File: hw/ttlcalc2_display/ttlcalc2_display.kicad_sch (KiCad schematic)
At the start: 21 parts, among them J1 DISP_CONN, J2 5V_PWR, J3 HV_PWR, J4 IO_BUS, Q1 MPSA42, Q2 MPSA42, Q3 MPSA42, U1 74LS93, U2 NE555P, U3 74LS08, U4 74LS139, U5 74LS173, U6 74LS138, U7 74LS173

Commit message: Continue work on display driver board schematic
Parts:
- added C50: 1000u, Capacitor_THT:CP_Radial_D10.0mm_P5.00mm, symbol Device:C_Polarized_US
- added C51: 100u, Capacitor_THT:CP_Radial_D18.0mm_P7.50mm, symbol Device:C_Polarized_US
- added U23: 74LS02, Package_DIP:DIP-14_W7.62mm, symbol 74xx:74LS02
- R1, R2, R3, R4, R5: footprint Resistor_THT:R_Axial_DIN0309_L9.0mm_D3.2mm_P2.54mm_Vertical -> Resistor_THT:R_Axial_DIN0207_L6.3mm_D2.5mm_P2.54mm_Vertical
- renumbered C1 to C101, C2 to C102, J4 to J2, J2 to J3, J3 to J4, U2 to U1, U1 to U2, U4 to U3, U6 to U4, U3 to U5, U5 to U6
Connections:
- net CLK2: now also U23.13; no longer J2.21 (Pin_21)
- net Digit Storage/~{WEN}: now also U23.4; no longer U3.4 (O0)
- net GND: now also C50.2, C51.2, U23.8
- net HT: now also C51.1
- net VCC: now also C50.1
- net CLK1: no longer names the net of J2.23 (Pin_23)
- net DI0: no longer names the net of J2.25 (Pin_25)
- net DI1: no longer names the net of J2.27 (Pin_27)
- net DI2: no longer names the net of J2.29 (Pin_29)
- net DI3: no longer names the net of J2.31 (Pin_31)
- net ~{RIO}: no longer names the net of J2.19 (Pin_19)
- new net: J2.21 (Pin_21), U23.9
- new net: U23.1, U23.5, U23.6
- new net: U23.3, U3.4 (O0)
- new net ~{CLK2}: U23.10, U23.11, U23.12, U23.2
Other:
- moved on the sheet: J2, J3, J4, U3A, U3B

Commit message: Simplify display driver board, add busy light
Removed digit storage and multiplexing logic from display driver, will handle in software instead
Add driver for busy indicator
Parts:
- removed C101: 10n, Capacitor_THT:C_Disc_D5.0mm_W2.5mm_P5.00mm, symbol Device:C
- removed C102: 47n, Capacitor_THT:C_Disc_D5.0mm_W2.5mm_P5.00mm, symbol Device:C
- removed C50: 1000u, Capacitor_THT:CP_Radial_D10.0mm_P5.00mm, symbol Device:C_Polarized_US
- removed C51: 100u, Capacitor_THT:CP_Radial_D18.0mm_P7.50mm, symbol Device:C_Polarized_US
- removed J3: 5V_PWR, TerminalBlock_Phoenix:TerminalBlock_Phoenix_MKDS-1,5-2-5.08_1x02_P5.08mm_Horizontal, symbol Connector_Generic:Conn_01x02
- removed J4: HV_PWR, TerminalBlock_Phoenix:TerminalBlock_Phoenix_MKDS-1,5-2-5.08_1x02_P5.08mm_Horizontal, symbol Connector_Generic:Conn_01x02
- removed R1: 39k, Resistor_THT:R_Axial_DIN0207_L6.3mm_D2.5mm_P2.54mm_Vertical, symbol Device:R_US
- removed R2: 3.3k, Resistor_THT:R_Axial_DIN0207_L6.3mm_D2.5mm_P2.54mm_Vertical, symbol Device:R_US
- removed U1: NE555P, Package_DIP:DIP-8_W7.62mm, symbol Timer:NE555P
- removed U2: 74LS93, Package_DIP:DIP-14_W7.62mm, symbol 74xx:74LS93
- removed U23: 74LS02, Package_DIP:DIP-14_W7.62mm, symbol 74xx:74LS02
- removed unit 4 of U5
- added Q4: MPSA42, Package_TO_SOT_THT:TO-92_Inline, symbol Transistor_BJT:MPSA42
- added R4: 27k, Resistor_THT:R_Axial_DIN0207_L6.3mm_D2.5mm_P2.54mm_Vertical, symbol Device:R_US
- added U3, U4: 74LS173, Package_DIP:DIP-16_W7.62mm, symbol 74xx:74LS173
- added unit 4 of U6
- renumbered R3 to R1, R4 to R2, R5 to R3, U3 to U1, U4 to U2, U7 to U5, U5 to U6, U6 to U7
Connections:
- net CLK2: now also U3.7 (Cp), U4.7 (Cp), U6.11
- net DO0: now also U3.14 (D0), U4.14 (D0)
- net DO1: now also U3.13 (D1), U4.13 (D1)
- net DO2: now also U3.12 (D2), U4.12 (D2)
- net DO3: now also U3.11 (D3), U4.11 (D3)
- net GND: now also Q4.1 (E), U3.1 (Oe1), U3.15 (Mr), U3.2 (Oe2), U3.8 (GND), U3.9 (E1), U4.1 (Oe1), U4.15 (Mr), U4.2 (Oe2), U4.8 (GND), U4.9 (E1)
- net NXSEL0: now also U3.3 (Q0)
- net NXSEL1: now also U3.4 (Q1)
- net NXSEL2: now also U3.5 (Q2)
- net NXSEL3: now also U3.6 (Q3)
- net VCC: now also U3.16 (VCC), U4.16 (VCC), U6.12
- net at U7.9 (E1): now also U2.13 (O2); no longer U2.15 (O0)
- net at J2.21 (Pin_21): now also U6.13
- net at U2.12 (O3): now also U5.9 (E1)
- net at U2.14 (O1): now also U4.10 (E2); no longer U5.9 (E1)
- net at U2.4 (E1): now also U1.4 (O0); no longer U1.5 (O1)
- net NE_BUSY: now reaches J1.40 (Pin_40)
- net NE_BUSY: now also Q4.3 (C)
- net BUSY: now reaches U5.6 (Q3)
- net BUSY: now also R4.1
- net Digit Storage/DOUT0 renamed Nixie Cathode Drive/NXD0
- net Nixie Cathode Drive/NXD0: now also U4.3 (Q0)
- net Digit Storage/DOUT1 renamed Nixie Cathode Drive/NXD1
- net Nixie Cathode Drive/NXD1: now also U4.4 (Q1)
- net Digit Storage/DOUT2 renamed Nixie Cathode Drive/NXD2
- net Nixie Cathode Drive/NXD2: now also U4.5 (Q2)
- net Digit Storage/DOUT3 renamed Nixie Cathode Drive/NXD3
- net Nixie Cathode Drive/NXD3: now also U4.6 (Q3)
- net Nixie Anode Drive/~{EN1} renamed Nixie Anode Drive/~{EN}
- new net: U2.15 (O0), U3.10 (E2)
- new net: Q4.2 (B), R4.2
- no-connect marks 20 -> 16
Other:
- removed sheet Digit Storage
- sheet Nixie Anode Drive ports: added ~{EN}; removed EN2, ~{EN1}
- moved on the sheet: Q1, Q2, Q3, R1, R2, R3, U1A, U1B, U2, U5

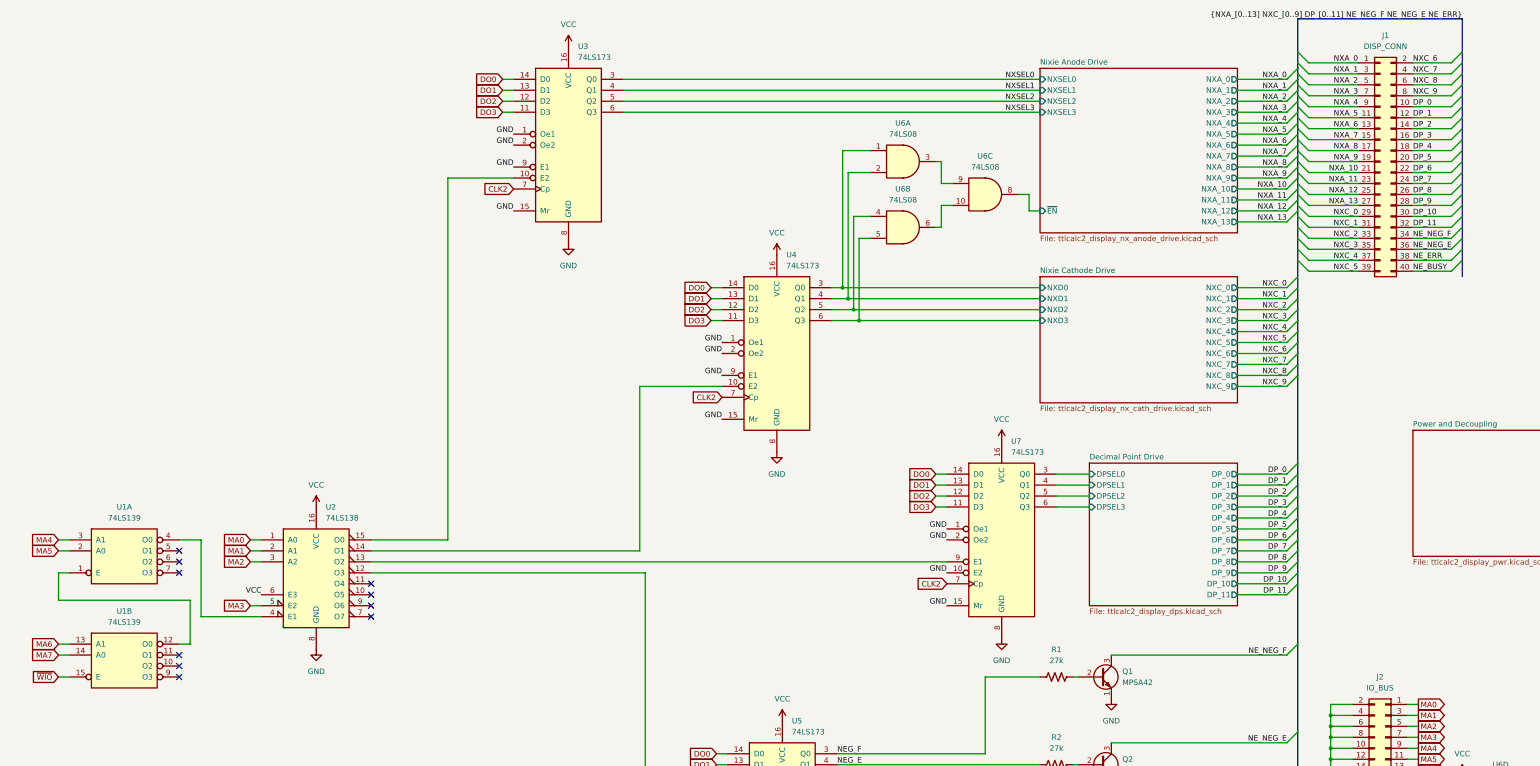
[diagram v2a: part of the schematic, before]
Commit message: Minor simplifications and ERC fix
Fix missing NE_BUSY from bus definition
Switch 74LS139 to 74LS138
Remove extra bypass caps
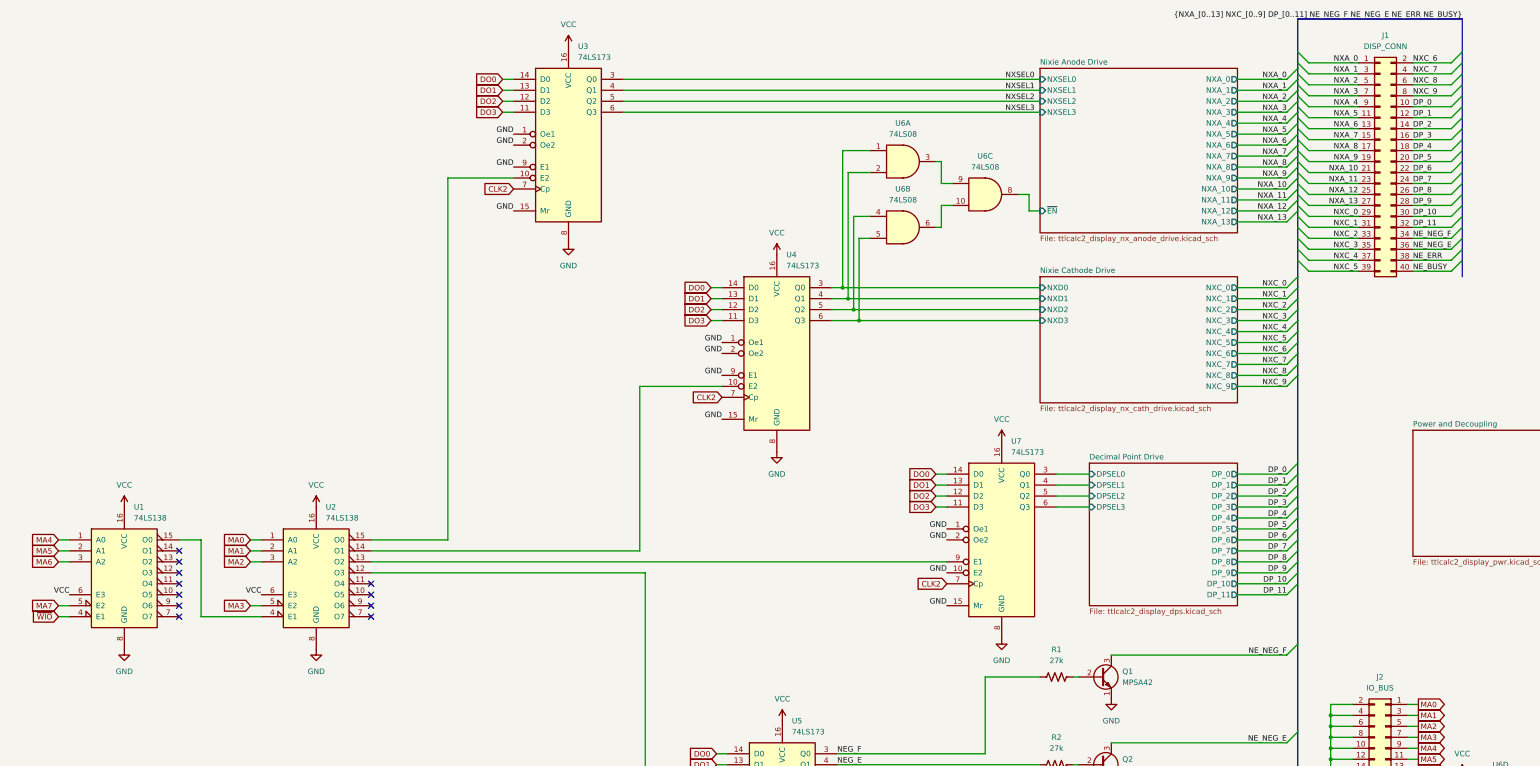
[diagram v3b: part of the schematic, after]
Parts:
- removed U1: 74LS139, Package_DIP:DIP-16_W7.62mm, symbol 74xx:74LS139
- added U1: 74LS138, Package_DIP:DIP-16_W7.62mm, symbol 74xx:74LS138
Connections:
- net GND: now also U1.8 (GND)
- net MA4: now also U1.1 (A0)
- net MA5: now also U1.2 (A1)
- net MA6: now also U1.3 (A2)
- net MA7: now also U1.5 (E2)
- net VCC: now also U1.16 (VCC), U1.6 (E3)
- net ~{WIO}: now also U1.4 (E1)
- net at U2.4 (E1): now also U1.15 (O0)
- no-connect marks 16 -> 17

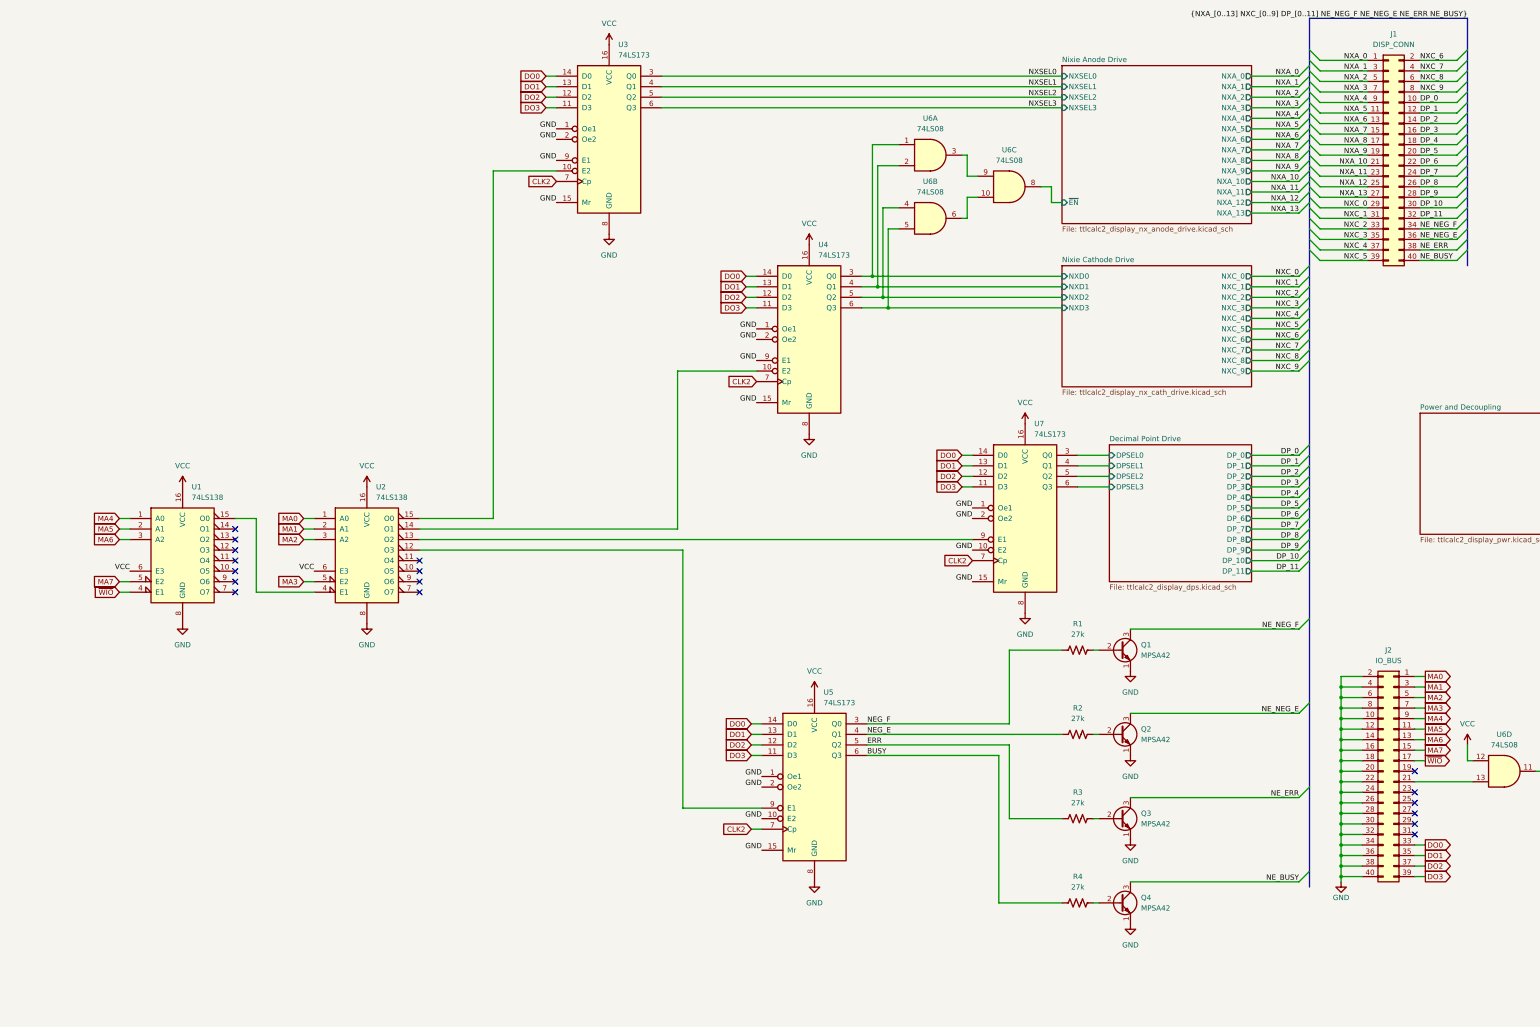
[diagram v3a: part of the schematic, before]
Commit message: Display driver board routing and silkscreen tweaks
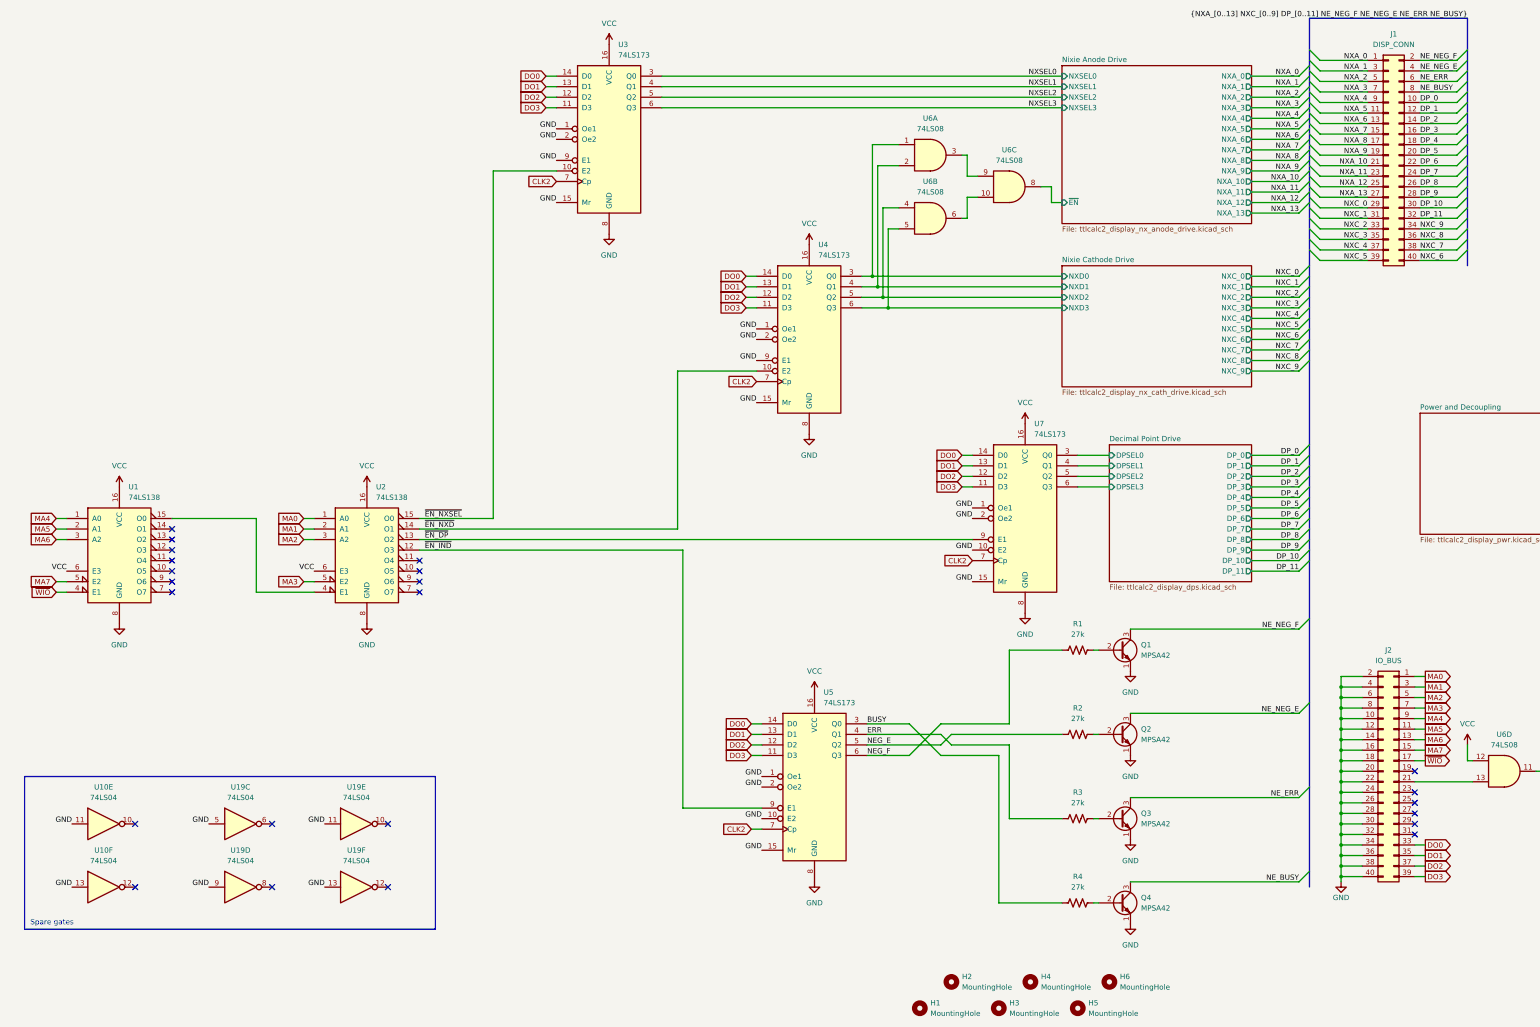
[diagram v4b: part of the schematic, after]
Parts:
- added H1, H2, H3, H4, H5, H6: MountingHole, MountingHole:MountingHole_3.2mm_M3, symbol Mechanical:MountingHole
- added U10, U19: 74LS04, Package_DIP:DIP-14_W7.62mm, symbol 74xx:74LS04
- J1: footprint Connector_PinHeader_2.54mm:PinHeader_2x20_P2.54mm_Vertical -> Connector_IDC:IDC-Header_2x20_P2.54mm_Vertical
- Q1, Q2, Q3, Q4: footprint Package_TO_SOT_THT:TO-92_Inline -> Package_TO_SOT_THT:TO-92_Inline_Wide
- R1, R2, R3, R4: footprint Resistor_THT:R_Axial_DIN0207_L6.3mm_D2.5mm_P2.54mm_Vertical -> Resistor_THT:R_Axial_DIN0207_L6.3mm_D2.5mm_P7.62mm_Horizontal
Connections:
- net BUSY: now also U5.3 (Q0); no longer U5.6 (Q3)
- net ERR: now also U5.4 (Q1); no longer U5.5 (Q2)
- net GND: now also U10.11, U10.13, U19.11, U19.13, U19.5, U19.9
- net NEG_E: now also U5.5 (Q2); no longer U5.4 (Q1)
- net NEG_F: now also U5.6 (Q3); no longer U5.3 (Q0)
- net NE_BUSY: now also J1.8 (Pin_8); no longer J1.40 (Pin_40)
- net NE_ERR: now also J1.6 (Pin_6); no longer J1.38 (Pin_38)
- net NE_NEG_E: now also J1.4 (Pin_4); no longer J1.36 (Pin_36)
- net NE_NEG_F: now also J1.2 (Pin_2); no longer J1.34 (Pin_34)
- net NXC_6: now also J1.40 (Pin_40); no longer J1.2 (Pin_2)
- net NXC_7: now also J1.38 (Pin_38); no longer J1.4 (Pin_4)
- net NXC_8: now also J1.36 (Pin_36); no longer J1.6 (Pin_6)
- net NXC_9: now also J1.34 (Pin_34); no longer J1.8 (Pin_8)
- net ~{EN_DP}: now reaches U2.13 (O2), U7.9 (E1)
- net ~{EN_NXSEL}: now reaches U2.15 (O0), U3.10 (E2)
- net ~{EN_IND}: now reaches U2.12 (O3), U5.9 (E1)
- net ~{EN_NXD}: now reaches U2.14 (O1), U4.10 (E2)
- no-connect marks 17 -> 23
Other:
- note added: "Spare gates"
- moved on the sheet: U1
